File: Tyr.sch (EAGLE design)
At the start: 208 parts, among them J1 TYR_TYR_DISPLAY, Q1 DTC123J, SW1 BUTTON, U1 STM32F303CC, U3 TYR_TPS2552, U4 CONTROLLER_PRTR5V0U2X, U5 MCP1700T, X1 CONTROLLER_USB-C-12PUSB-C-12P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, Y1 8Mhz

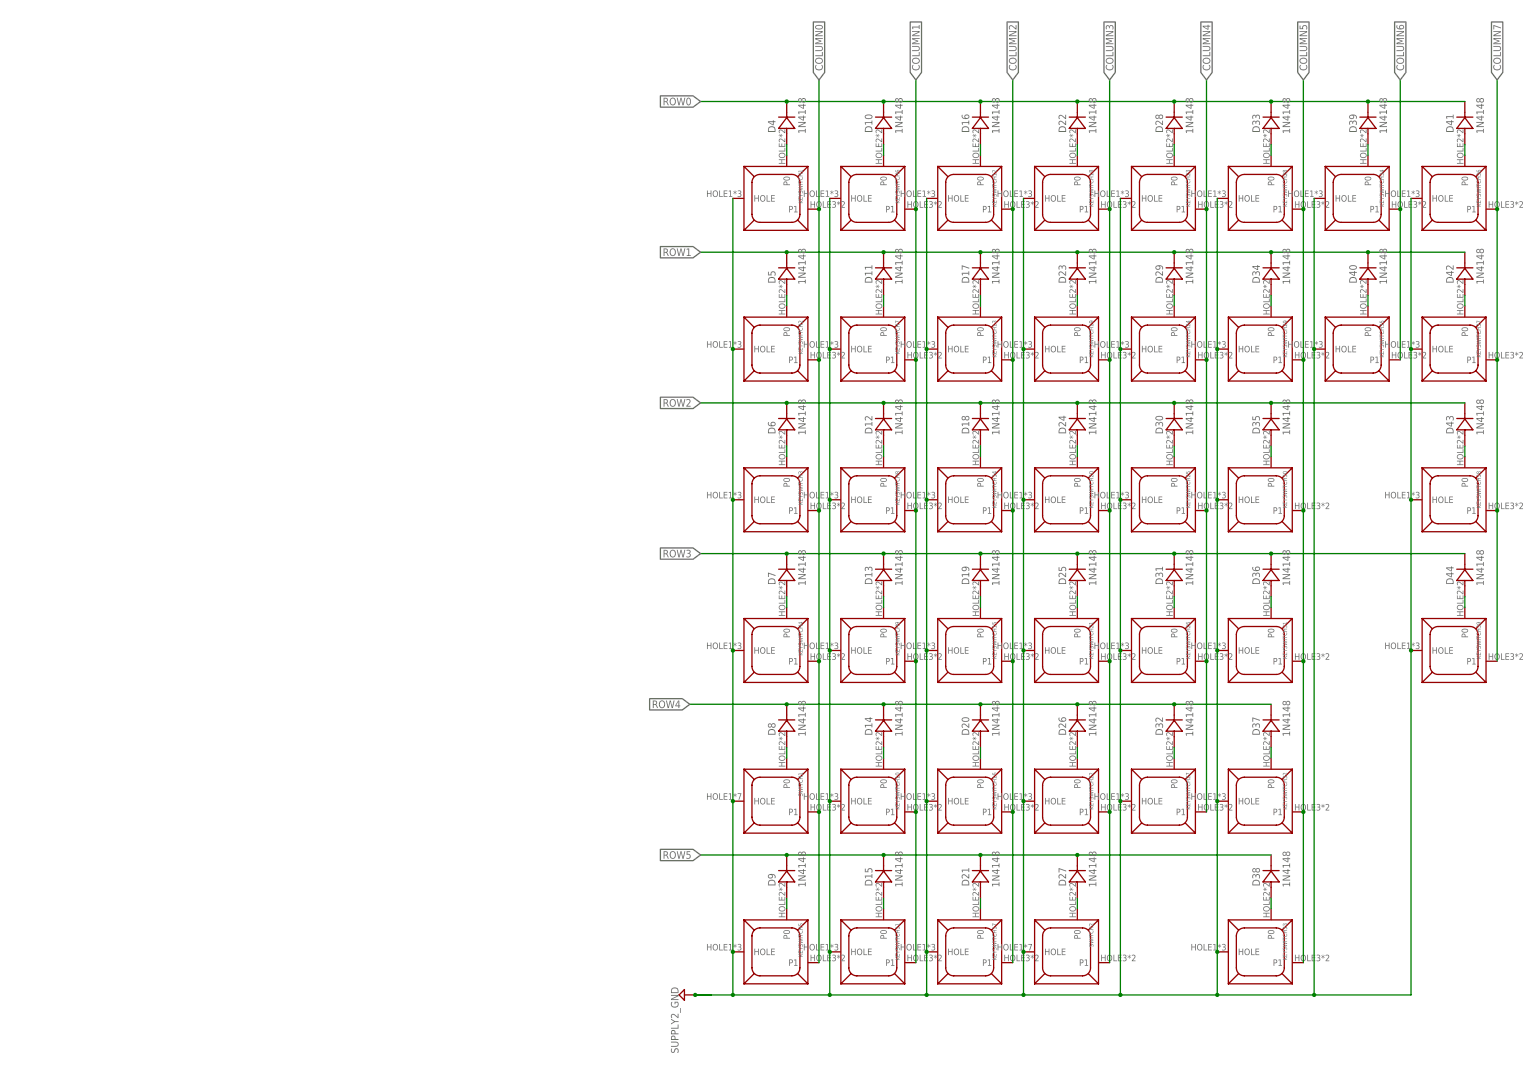
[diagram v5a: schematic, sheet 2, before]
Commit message: Y branching & renumber
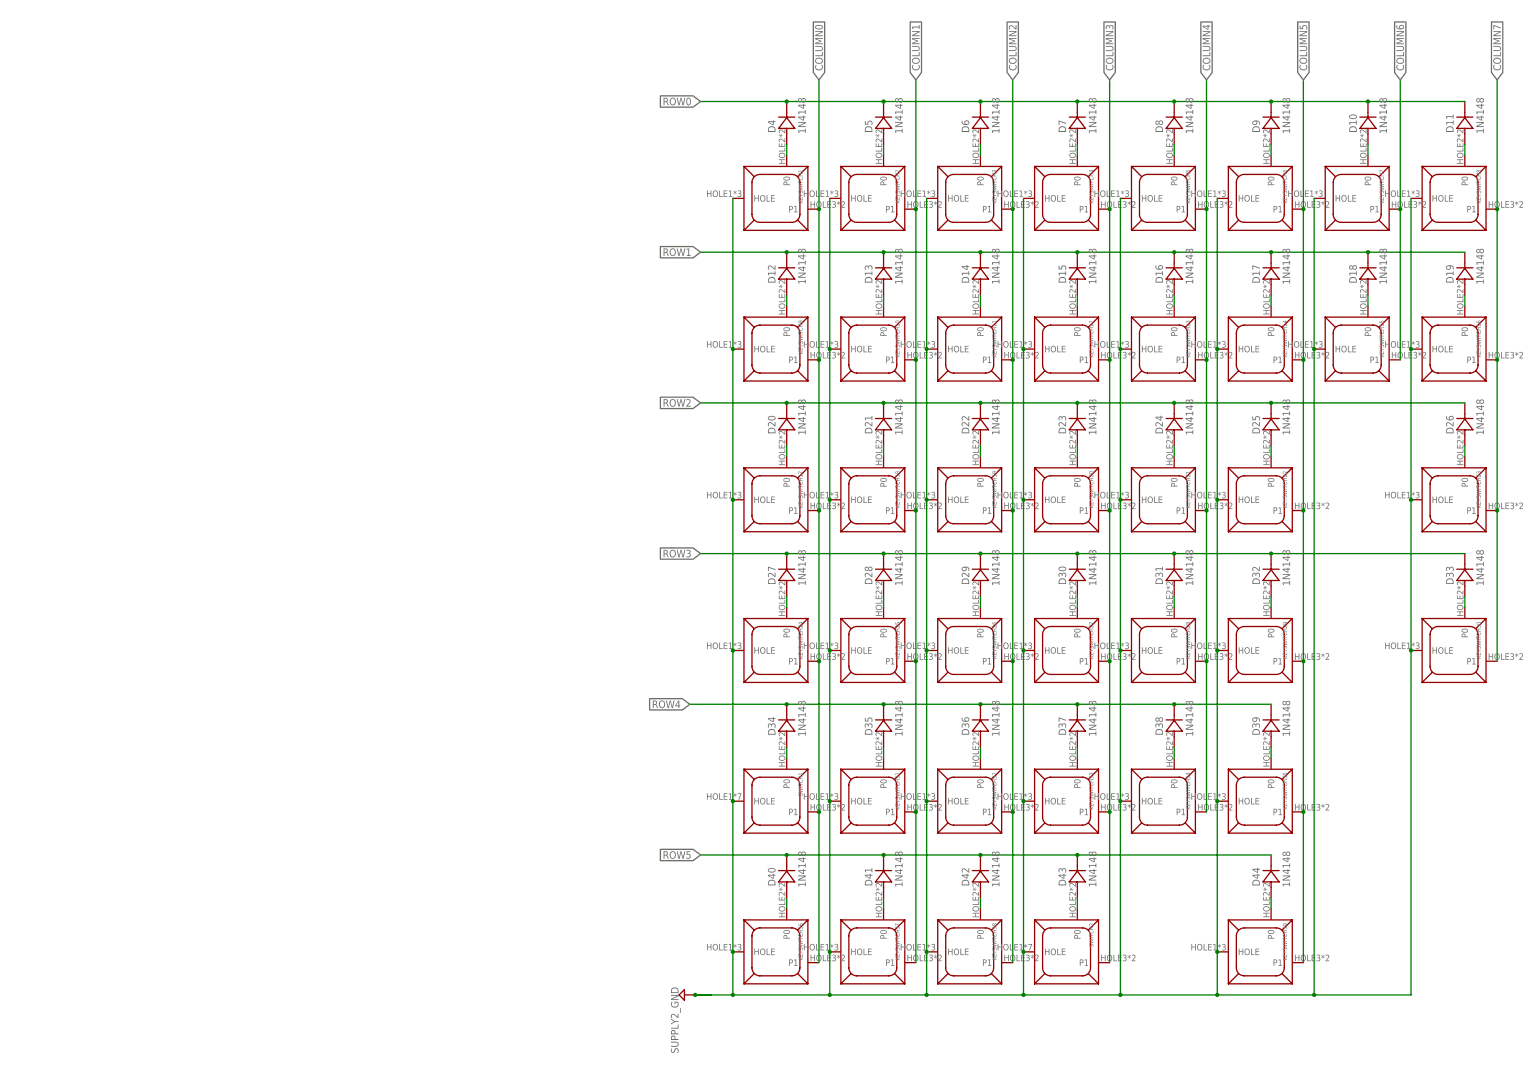
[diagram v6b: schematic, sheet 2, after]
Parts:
- removed U$1: MB85RC256V, Tyr:MB85RC256V
- added U6: TYR_TPS2552, Tyr:TYR_TPS2552
- C1: value 10n -> 100n
- C10: value 22p -> 10u
- C11: value 4.7n -> 22p
- C12: value 10u -> 22p
- C13: value 100n -> 10u
- C14: value 100n -> 0.1u
- C15: value 104 -> 0.1u
- C2: value 1u -> 100n
- C3: value 0.1u -> 10n
- C4: value 100n -> 1u
- C50: value 10u -> 104
- C6: value 100n -> 4.7u
- C7: value 4.7u -> 100n
- C8: value 0.1u -> 100n
- C9: value 22p -> 4.7n
- KEYSWITCH24: value KEYBOARD_KEYSWITCH-MX-1U-HOTSWAP -> KEYBOARD_KEYSWITCH-MX-1U-HOTSWAPCAPSLOCK; device Tyr:KEYBOARD_KEYSWITCH-MX-1U-HOTSWAP -> Tyr:KEYBOARD_KEYSWITCH-MX-1U-HOTSWAPCAPSLOCK
- KEYSWITCH4: value KEYBOARD_KEYSWITCH-MX-1U-HOTSWAPCAPSLOCK -> KEYBOARD_KEYSWITCH-MX-1U-HOTSWAP; device Tyr:KEYBOARD_KEYSWITCH-MX-1U-HOTSWAPCAPSLOCK -> Tyr:KEYBOARD_KEYSWITCH-MX-1U-HOTSWAP
- R1: value 0.1/1% (PT2512FK-070R1L) -> 5.1k; device Tyr:MICROBUILDER_RESISTOR2512 -> Tyr:COMPONENTS_RESISTOR-0603
- R11: value 10k -> 0.1/1% (PT2512FK-070R1L); device Tyr:COMPONENTS_RESISTOR-0603 -> Tyr:MICROBUILDER_RESISTOR2512
- R12: value 10k -> 54.9k
- R2: value 100k -> 22
- R3: value 10k -> 22
- R4: value 100k -> 5.1k
- R5: value 54.9k -> 10k
- R6: value 22 -> 10k
- R7: value 22 -> 100k
- R8: value 5.1k -> 100k
- R9: value 5.1k -> 10k
- U1: value STM32F303CC -> MCP1700T; device Tyr:STM32F303CC -> Tyr:MCP1700T
- U2: value (none) -> CONTROLLER_PRTR5V0U2X; device Tyr:MICROBUILDER_INA219 -> Tyr:CONTROLLER_PRTR5V0U2X
- U3: value TYR_TPS2552 -> STM32F303CC; device Tyr:TYR_TPS2552 -> Tyr:STM32F303CC
- U4: value CONTROLLER_PRTR5V0U2X -> MB85RC256V; device Tyr:CONTROLLER_PRTR5V0U2X -> Tyr:MB85RC256V
- U5: value MCP1700T -> (none); device Tyr:MCP1700T -> Tyr:MICROBUILDER_INA219
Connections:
- removed net N$11 (its old number): D10.A, KEYSWITCH6.P0
- removed net N$12 (its old number): D16.A, KEYSWITCH12.P0
- removed net N$13 (its old number): D22.A, KEYSWITCH18.P0
- removed net N$48 (its old number): D38.A, KEYSWITCH33.P0
- new net N$24: D12.A, KEYSWITCH9.P0
- new net N$31: D20.A, KEYSWITCH17.P0
- new net N$32: D27.A, KEYSWITCH24.P0
- new net N$38: D33.A, KEYSWITCH30.P0
- net 3.3V: now also C10.2, C15.2, C3.1, C8.2, D1.A, R5.2, R6.2, R9.2, U1.VO, U3.VBAT, U3.VCC, U3.VCC/VDDA/VREF+, U3.VCC1, U3.VCC2, U4.VCC, U5.VCC; no longer C14.2, C3.2, C50.2, C7.1, D3.A, R11.2, R12.2, R13.2, U$1.VCC, U1.VBAT, U1.VCC, U1.VCC/VDDA/VREF+, U1.VCC1, U1.VCC2, U2.VCC, U5.VO
- net BOOT0: now also C13.2, D3.C, R7.1, U3.BOOT0; no longer C12.2, D1.C, R4.1, U1.BOOT0
- net COLUMN0: now also KEYSWITCH17.P1, KEYSWITCH24.P1, KEYSWITCH36.P1, KEYSWITCH9.P1, U3.DAC1-OUT2/PA5; no longer KEYSWITCH2.P1, KEYSWITCH3.P1, KEYSWITCH4.P1, KEYSWITCH5.P1, U1.DAC1-OUT2/PA5
- net COLUMN1: now also KEYSWITCH18.P1, KEYSWITCH2.P1, KEYSWITCH25.P1, KEYSWITCH31.P1, KEYSWITCH37.P1, U3.PA6; no longer KEYSWITCH11.P1, KEYSWITCH6.P1, KEYSWITCH7.P1, KEYSWITCH8.P1, KEYSWITCH9.P1, U1.PA6
- net COLUMN2: now also KEYSWITCH11.P1, KEYSWITCH19.P1, KEYSWITCH26.P1, KEYSWITCH3.P1, KEYSWITCH32.P1, KEYSWITCH38.P1, U3.PA7; no longer KEYSWITCH12.P1, KEYSWITCH13.P1, KEYSWITCH14.P1, KEYSWITCH15.P1, KEYSWITCH16.P1, KEYSWITCH17.P1, U1.PA7
- net COLUMN3: now also KEYSWITCH12.P1, KEYSWITCH27.P1, KEYSWITCH33.P1, KEYSWITCH4.P1, U3.PB0; no longer KEYSWITCH18.P1, KEYSWITCH19.P1, KEYSWITCH21.P1, KEYSWITCH22.P1, U1.PB0
- net COLUMN4: now also KEYSWITCH13.P1, KEYSWITCH21.P1, KEYSWITCH28.P1, KEYSWITCH34.P1, KEYSWITCH5.P1, U3.PB1; no longer KEYSWITCH23.P1, KEYSWITCH24.P1, KEYSWITCH25.P1, KEYSWITCH26.P1, KEYSWITCH27.P1, U1.PB1
- net COLUMN5: now also KEYSWITCH14.P1, KEYSWITCH22.P1, KEYSWITCH35.P1, KEYSWITCH39.P1, KEYSWITCH6.P1, U3.PB10; no longer KEYSWITCH28.P1, KEYSWITCH30.P1, KEYSWITCH31.P1, KEYSWITCH32.P1, KEYSWITCH33.P1, U1.PB10
- net COLUMN6: now also KEYSWITCH15.P1, KEYSWITCH7.P1, U3.PB11; no longer KEYSWITCH34.P1, KEYSWITCH35.P1, U1.PB11
- net COLUMN7: now also KEYSWITCH16.P1, KEYSWITCH23.P1, KEYSWITCH30.P1, KEYSWITCH8.P1, U3.PB12; no longer KEYSWITCH36.P1, KEYSWITCH37.P1, KEYSWITCH38.P1, KEYSWITCH39.P1, U1.PB12
- net D+: now also R3.2, U3.PA12/USB_DP; no longer R7.2, U1.PA12/USB_DP
- net D-: now also R2.2, U3.PA11/USB_DM; no longer R6.2, U1.PA11/USB_DM
- net GND: now also C11.1, C3.2, C7.1, C9.2, R1.2, R12.1, R13.1, R7.2, U2.1, U3.GND/VSSA/VREF-, U3.GND1, U3.GND2, U4.GND, U6.GND; no longer C11.2, C3.1, C7.2, C9.1, R3.1, R5.1, R8.2, R9.2, U$1.GND, U1.GND/VSSA/VREF-, U1.GND1, U1.GND2, U2.GND, U4.1
- net LED_DATA: now also LED41.DI, U3.DAC1-OUT1/PA4; no longer LED35.DI, U1.DAC1-OUT1/PA4
- net LED_ENABLE: now also R13.2, U3.PA1, U6.EN; no longer R3.2, U1.PA1, U3.EN
- net LED_FAULT: now also R8.1, U3.PA2, U6.FAULT; no longer R2.1, U1.PA2, U3.FAULT
- net LED_VCC: now also C50.2, U6.OUT; no longer C15.2, U3.OUT
- net N$1: now also D13.A, KEYSWITCH10.P0; no longer D11.A, KEYSWITCH7.P0
- net N$14: now also D8.A, KEYSWITCH5.P0; no longer D28.A, KEYSWITCH23.P0
- net N$15: now also D9.A, KEYSWITCH6.P0; no longer D33.A, KEYSWITCH28.P0
- net N$16: now also D10.A, KEYSWITCH7.P0; no longer D39.A, KEYSWITCH34.P0
- net N$17: now also D11.A, KEYSWITCH8.P0; no longer D41.A, KEYSWITCH36.P0
- net N$18: now also D19.A, KEYSWITCH16.P0; no longer D42.A, KEYSWITCH37.P0
- net N$19: now also D18.A, KEYSWITCH15.P0; no longer D40.A, KEYSWITCH35.P0
- net N$2: now also R11.2, U5.VIN-, U6.IN; no longer R1.2, U2.VIN-, U3.IN
- net N$20: now also D17.A, KEYSWITCH14.P0; no longer D34.A, KEYSWITCH29.P0
- net N$21: now also D16.A, KEYSWITCH13.P0; no longer D29.A, KEYSWITCH24.P0
- net N$22: now also D15.A, KEYSWITCH12.P0; no longer D23.A, KEYSWITCH19.P0
- net N$23: now also D14.A, KEYSWITCH11.P0; no longer D17.A, KEYSWITCH13.P0
- net N$25: now also D26.A, KEYSWITCH23.P0; no longer D43.A, KEYSWITCH38.P0
- net N$26: now also D25.A, KEYSWITCH22.P0; no longer D35.A, KEYSWITCH30.P0
- net N$27: now also D24.A, KEYSWITCH21.P0; no longer D30.A, KEYSWITCH25.P0
- net N$28: now also D23.A; no longer D24.A
- net N$29: now also D22.A, KEYSWITCH19.P0; no longer D18.A, KEYSWITCH14.P0
- net N$3: now also R12.2, U6.ILIM; no longer R5.2, U3.ILIM
- net N$30: now also LED39.DI, LED40.DO; no longer LED18.DI, LED24.DO
- net N$33: now also D28.A, KEYSWITCH25.P0; no longer D13.A, KEYSWITCH9.P0
- net N$34: now also D29.A, KEYSWITCH26.P0; no longer D19.A, KEYSWITCH15.P0
- net N$35: now also D30.A, KEYSWITCH27.P0; no longer D25.A, KEYSWITCH21.P0
- net N$36: now also KEYSWITCH28.P0; no longer KEYSWITCH26.P0
- net N$37: now also D32.A, KEYSWITCH29.P0; no longer D36.A, KEYSWITCH31.P0
- net N$39: now also D39.A, KEYSWITCH35.P0; no longer D37.A, KEYSWITCH32.P0
- net N$4: now also R1.1; no longer R8.1
- net N$40: now also D37.A, KEYSWITCH33.P0; no longer D26.A, KEYSWITCH22.P0
- net N$41: now also D36.A, KEYSWITCH32.P0; no longer D20.A, KEYSWITCH16.P0
- net N$42: now also D35.A, KEYSWITCH31.P0; no longer D14.A, KEYSWITCH10.P0
- net N$43: now also D34.A; no longer D8.A
- net N$44: now also D40.A, KEYSWITCH36.P0; no longer D9.A, KEYSWITCH5.P0
- net N$45: now also D41.A, KEYSWITCH37.P0; no longer D15.A, KEYSWITCH11.P0
- net N$46: now also D42.A, KEYSWITCH38.P0; no longer D21.A, KEYSWITCH17.P0
- net N$47: now also D43.A; no longer D27.A
- net N$49: now also D38.A, KEYSWITCH34.P0; no longer D32.A, KEYSWITCH27.P0
- net N$5: now also D3.A; no longer D1.A
- net N$50: now also D21.A, KEYSWITCH18.P0; no longer D12.A, KEYSWITCH8.P0
- net N$51: now also LED38.DI, LED39.DO; no longer LED12.DI, LED18.DO
- net N$52: now also LED37.DI, LED38.DO; no longer LED12.DO, LED6.DI
- net N$53: now also LED36.DI, LED37.DO; no longer LED34.DI, LED6.DO
- net N$54: now also LED35.DI, LED36.DO; no longer LED29.DI, LED34.DO
- net N$55: now also LED34.DI, LED35.DO; no longer LED23.DI, LED29.DO
- net N$56: now also LED33.DI, LED34.DO; no longer LED17.DI, LED23.DO
- net N$57: now also LED32.DI, LED33.DO; no longer LED11.DI, LED17.DO
- net N$58: now also LED31.DI, LED32.DO; no longer LED11.DO, LED5.DI
- net N$59: now also LED30.DI, LED31.DO; no longer LED41.DI, LED5.DO
- net N$6: now also R2.1, U2.3; no longer R6.1, U4.3
- net N$60: now also LED29.DI, LED30.DO; no longer LED33.DI, LED41.DO
- net N$61: now also LED29.DO; no longer LED33.DO
- net N$62: now also LED27.DI; no longer LED22.DI
- net N$63: now also LED26.DI, LED27.DO; no longer LED16.DI, LED22.DO
- net N$64: now also LED25.DI, LED26.DO; no longer LED10.DI, LED16.DO
- net N$65: now also LED24.DI, LED25.DO; no longer LED10.DO, LED4.DI
- net N$66: now also LED23.DI, LED24.DO; no longer LED4.DO, LED40.DI
- net N$67: now also LED22.DI, LED23.DO; no longer LED32.DI, LED40.DO
- net N$68: now also LED21.DI, LED22.DO; no longer LED27.DI, LED32.DO
- net N$69: now also LED20.DI, LED21.DO; no longer LED21.DI, LED27.DO
- net N$7: now also R3.1, U2.2; no longer R7.1, U4.2
- net N$70: now also LED19.DI, LED20.DO; no longer LED15.DI, LED21.DO
- net N$71: now also LED18.DI, LED19.DO; no longer LED15.DO, LED9.DI
- net N$72: now also LED17.DI, LED18.DO; no longer LED3.DI, LED9.DO
- net N$73: now also LED16.DI, LED17.DO; no longer LED3.DO, LED39.DI
- net N$74: now also LED15.DI, LED16.DO; no longer LED37.DI, LED39.DO
- net N$75: now also LED14.DI, LED15.DO; no longer LED31.DI, LED37.DO
- net N$76: now also LED13.DI, LED14.DO; no longer LED26.DI, LED31.DO
- net N$77: now also LED12.DI, LED13.DO; no longer LED20.DI, LED26.DO
- net N$78: now also LED11.DI, LED12.DO; no longer LED14.DI, LED20.DO
- net N$79: now also LED10.DI, LED11.DO; no longer LED14.DO, LED8.DI
- net N$80: now also LED10.DO, LED9.DI; no longer LED2.DI, LED8.DO
- net N$81: now also LED8.DI, LED9.DO; no longer LED2.DO, LED38.DI
- net N$82: now also LED7.DI, LED8.DO; no longer LED36.DI, LED38.DO
- net N$83: now also LED6.DI, LED7.DO; no longer LED30.DI, LED36.DO
- net N$84: now also LED5.DI, LED6.DO; no longer LED25.DI, LED30.DO
- net N$85: now also LED4.DI, LED5.DO; no longer LED19.DI, LED25.DO
- net N$86: now also LED3.DI, LED4.DO; no longer LED13.DI, LED19.DO
- net N$87: now also LED2.DI, LED3.DO; no longer LED13.DO, LED7.DI
- net N$88: now also LED2.DO; no longer LED7.DO
- net N$89: now also R4.1; no longer R9.1
- net N$9: now also LED40.DI, LED41.DO; no longer LED24.DI, LED35.DO
- net NRST: now also C9.1, U3.NRST; no longer C11.1, U1.NRST
- net ROW0: now also D11.C, D5.C, D6.C, D7.C, D8.C, D9.C, U3.PA8; no longer D16.C, D22.C, D28.C, D33.C, D39.C, D41.C, U1.PA8
- net ROW1: now also D12.C, D13.C, D14.C, D15.C, D16.C, D18.C, D19.C, U3.PB15; no longer D11.C, D23.C, D29.C, D34.C, D40.C, D42.C, D5.C, U1.PB15
- net ROW2: now also D20.C, D21.C, D22.C, D23.C, D25.C, D26.C, U3.PB14; no longer D12.C, D18.C, D30.C, D35.C, D43.C, D6.C, U1.PB14
- net ROW3: now also D27.C, D28.C, D29.C, D30.C, D32.C, D33.C, U3.PB13; no longer D13.C, D19.C, D25.C, D36.C, D44.C, D7.C, U1.PB13
- net ROW4: now also D34.C, D35.C, D36.C, D38.C, D39.C, U3.PB2; no longer D14.C, D20.C, D26.C, D32.C, D8.C, U1.PB2
- net ROW5: now also D40.C, D41.C, D42.C, D43.C, D44.C, U3.PA3; no longer D15.C, D21.C, D27.C, D38.C, D9.C, U1.PA3
- net SCL: now also R5.1, R9.1, U3.I2C2_SCL/PA9, U4.SCL, U5.SCL; no longer R10.1, R12.1, U$1.SCL, U1.I2C2_SCL/PA9, U2.SCL
- net SDA: now also R10.1, R6.1, U3.I2C2_SDA/PA10, U4.SDA, U5.SDA; no longer R11.1, R13.1, U$1.SDA, U1.I2C2_SDA/PA10, U2.SDA
- net SWCLK: now also U3.PA14/SWCLK-JTCK/I2C1_SDA; no longer U1.PA14/SWCLK-JTCK/I2C1_SDA
- net SWDIO: now also U3.PA13/SWDIO-JTMS; no longer U1.PA13/SWDIO-JTMS
- net VCC: now also C14.2, C7.2, D1.C, R11.1, R8.2, U1.VI, U2.4, U5.VIN+; no longer C13.2, C8.2, D3.C, R1.1, R2.2, U2.VIN+, U4.4, U5.VI
- net XTAL1: now also C11.2, U3.PF0/OSC_IN/12C2_SDA; no longer C9.2, U1.PF0/OSC_IN/12C2_SDA
- net XTAL2: now also C12.2, U3.PF1/OSC_OUT/I2C2_SCL; no longer C10.2, U1.PF1/OSC_OUT/I2C2_SCL
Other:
- moved on the sheet: C1, C10, C11, C12, C13, C14, C16, C17, C18, C19, C2, C20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

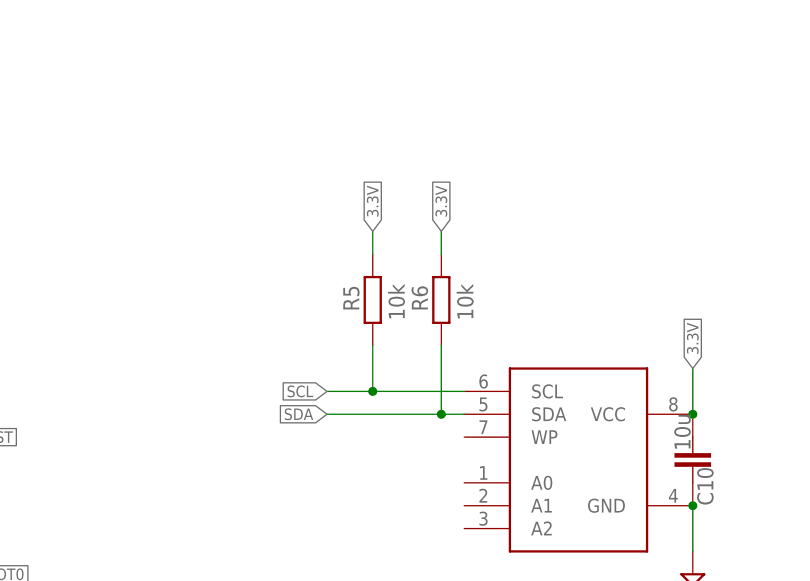
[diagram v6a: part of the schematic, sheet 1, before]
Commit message: Remove uneccessary power to I2C
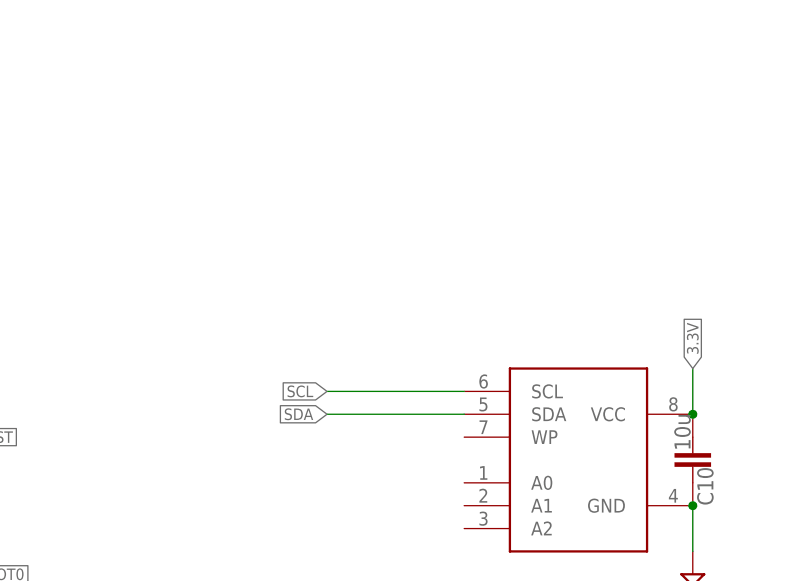
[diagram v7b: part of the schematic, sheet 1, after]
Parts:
- removed R5, R6: 10k, Tyr:COMPONENTS_RESISTOR-0603
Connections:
- net 3.3V: no longer R5.2, R6.2
- net SCL: no longer R5.1
- net SDA: no longer R6.1
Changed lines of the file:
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@@
 <part name="SUPPLY14" library="Tyr" library_urn="urn:adsk.eagle:library:14733090" deviceset="SUPPLY2_GND" device=""/>
 <part name="C10" library="Tyr" library_urn="urn:adsk.eagle:library:14733090" deviceset="COMPONENTS_CAPACITOR" device="-0603" package3d_urn="urn:adsk.eagle:package:14733142/2" value="10u"/>
-<part name="R5" library="Tyr" library_urn="urn:adsk.eagle:library:14733090" deviceset="COMPONENTS_RESISTOR" device="-0603" package3d_urn="urn:adsk.eagle:package:14733141/2" value="10k"/>
-<part name="R6" library="Tyr" library_urn="urn:adsk.eagle:library:14733090" deviceset="COMPONENTS_RESISTOR" device="-0603" package3d_urn="urn:adsk.eagle:package:14733141/2" value="10k"/>
 <part name="R9" library="Tyr" library_urn="urn:adsk.eagle:library:14733090" deviceset="COMPONENTS_RESISTOR" device="-0603" package3d_urn="urn:adsk.eagle:package:14733141/2" value="10k"/>
 <part name="R10" library="Tyr" library_urn="urn:adsk.eagle:library:14733090" deviceset="COMPONENTS_RESISTOR" device="-0603" package3d_urn="urn:adsk.eagle:package:14733141/2" value="10k"/>
@@
 <attribute name="VALUE" x="342.646" y="138.176" size="1.778" layer="96" rot="MR90" align="top-left"/>
 </instance>
-<instance part="R5" gate="G$1" x="307.34" y="154.94" smashed="yes" rot="R90">
-<attribute name="NAME" x="305.8414" y="153.67" size="1.778" layer="95" rot="R90"/>
-<attribute name="VALUE" x="310.896" y="152.654" size="1.778" layer="96" rot="R90"/>
-</instance>
-<instance part="R6" gate="G$1" x="314.96" y="154.94" smashed="yes" rot="R90">
-<attribute name="NAME" x="313.4614" y="153.67" size="1.778" layer="95" rot="R90"/>
-<attribute name="VALUE" x="318.516" y="152.654" size="1.778" layer="96" rot="R90"/>
-</instance>
 <instance part="R9" gate="G$1" x="55.88" y="48.26" smashed="yes" rot="R90">
 <attribute name="NAME" x="54.3814" y="46.99" size="1.778" layer="95" rot="R90"/>
@@
 <segment>
 <pinref part="U4" gate="G$1" pin="SDA"/>
-<wire x1="317.5" y1="142.24" x2="314.96" y2="142.24" width="0.1524" layer="91"/>
 <label x="302.26" y="142.24" size="1.27" layer="95" rot="R180" xref="yes"/>
-<pinref part="R6" gate="G$1" pin="1"/>
-<wire x1="314.96" y1="142.24" x2="302.26" y2="142.24" width="0.1524" layer="91"/>
-<wire x1="314.96" y1="149.86" x2="314.96" y2="142.24" width="0.1524" layer="91"/>
-<junction x="314.96" y="142.24"/>
+<wire x1="317.5" y1="142.24" x2="302.26" y2="142.24" width="0.1524" layer="91"/>
 </segment>
 </net>
@@
 <segment>
 <pinref part="U4" gate="G$1" pin="SCL"/>
-<wire x1="317.5" y1="144.78" x2="307.34" y2="144.78" width="0.1524" layer="91"/>
+<wire x1="317.5" y1="144.78" x2="302.26" y2="144.78" width="0.1524" layer="91"/>
 <label x="302.26" y="144.78" size="1.27" layer="95" rot="R180" xref="yes"/>
-<pinref part="R5" gate="G$1" pin="1"/>
-<wire x1="307.34" y1="144.78" x2="302.26" y2="144.78" width="0.1524" layer="91"/>
-<wire x1="307.34" y1="149.86" x2="307.34" y2="144.78" width="0.1524" layer="91"/>
-<junction x="307.34" y="144.78"/>
 </segment>
 </net>
@@
 <junction x="342.9" y="142.24"/>
 </segment>
-<segment>
-<pinref part="R5" gate="G$1" pin="2"/>
-<wire x1="307.34" y1="160.02" x2="307.34" y2="162.56" width="0.1524" layer="91"/>
-<label x="307.34" y="162.56" size="1.27" layer="95" rot="R90" xref="yes"/>
-</segment>
-<segment>
-<pinref part="R6" gate="G$1" pin="2"/>
-<wire x1="314.96" y1="160.02" x2="314.96" y2="162.56" width="0.1524" layer="91"/>
-<label x="314.96" y="162.56" size="1.27" layer="95" rot="R90" xref="yes"/>
-</segment>
-</net>
+</net>

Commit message: Update logo
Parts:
- added U$1: LOGO_TYR, Tyr:LOGO_TYR
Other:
- note added: "5V to 3.3V Regulator"
- note added: "DFU Hard Reset Circuit"
- note added: "I2C FRAM Module"
- note added: "MCU & Crystal"
- note added: "RGB Current Monitoring & Limiting"
- note added: "Type-C & ESD Protection"
- moved on the sheet: C10, C13, C14, C15, C7, C8, C9, D1, D2, D3, PH1, Q1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
